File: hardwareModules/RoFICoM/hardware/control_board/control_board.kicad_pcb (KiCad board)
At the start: 4 copper layers, 193.2 x 52.8 mm, 91 parts, among them J1 SkirtConnector, J10 SENSE_A, J11 SENSE_B, J12 SENSE_1, J13 SENSE_2, J14 48V_A, J15 48V_1, J16 48V_B, J17 48V_2, J18 GND_A, J19 GND_1, J2 M+, J20 GND_B, J21 GND_2, J22 RX_A, J23 RX_B, J24 TX_1, J25 TX_2, J26 BoardSkirtConnector, J27 SkirtConnector, J28 SkirtConnector, J3 M-, J4 SYS_CONN, J5 PWR_CONN_1, J6 PWR_CONN_2, J7 SIDE_1, J8 SIDE_2, J9 SIDE_3, Q1 AP20P30Q, Q2 PNM723T703E0-2, Q3 AP20P30Q, Q4 AP20P30Q, Q5 PNM723T703E0-2, Q6 AP20P30Q, U2 DRV8837C, U3 HX6306P332MR, U6 ACS70331, U7 ACS70331, U8 VL53L1X, U9 STM32G071CBUx

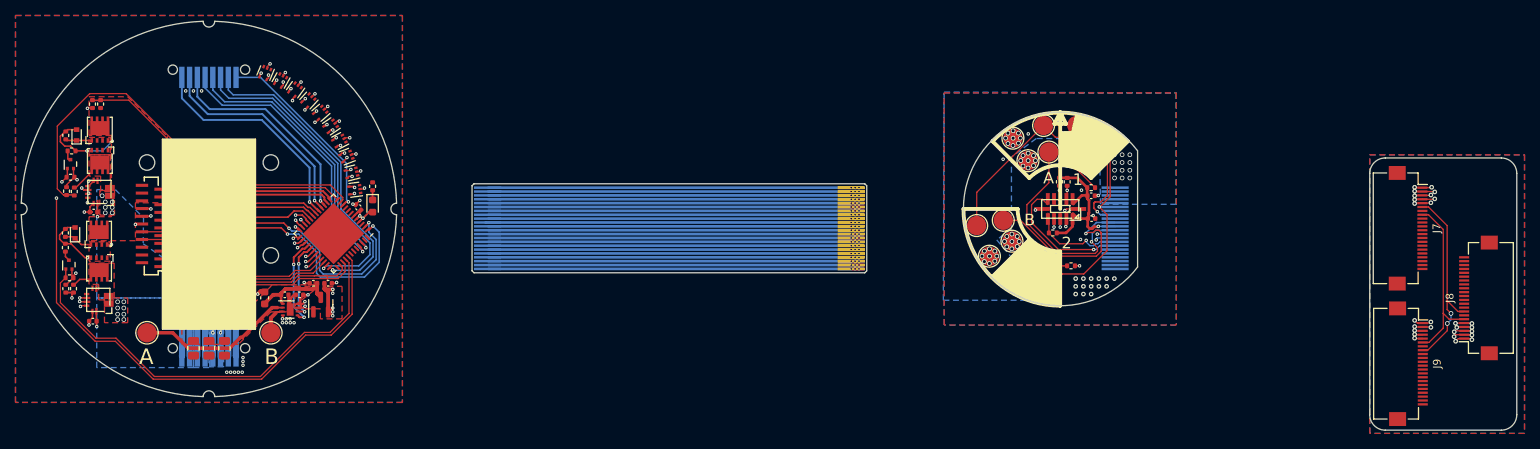
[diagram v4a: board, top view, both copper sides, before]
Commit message: roficom: Add Hall position sensor hardware
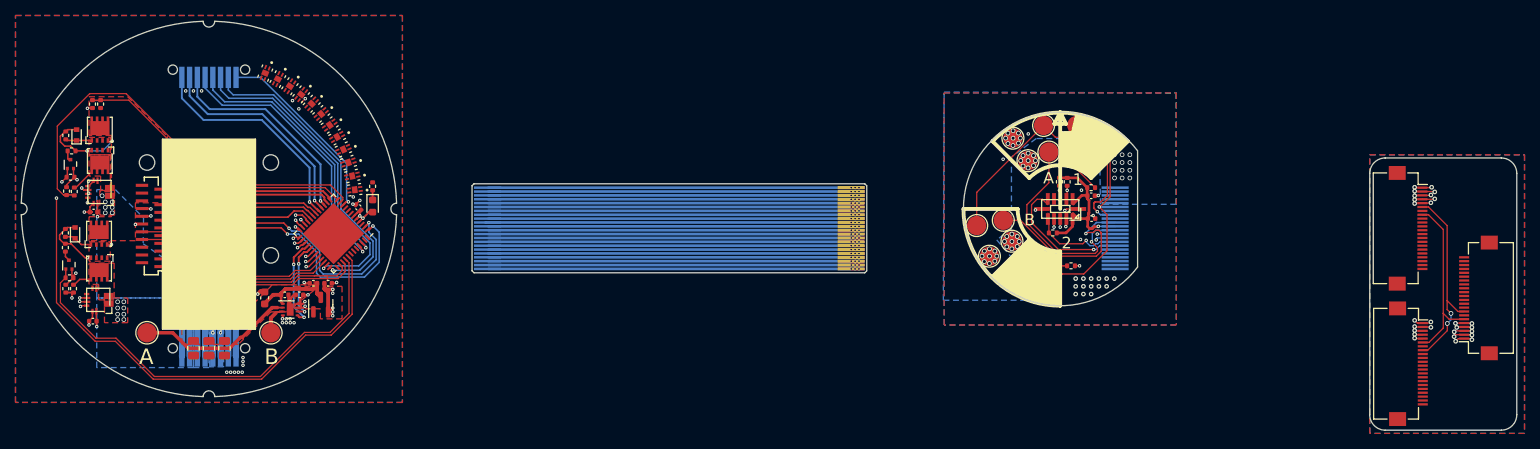
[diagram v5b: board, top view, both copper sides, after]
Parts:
- added HAL11: TMAG5231C1GQDMRR, rofi:X2SON_31H1DQDMRR_TEX, F.Cu at (98.5, 85.7)
- added HAL12: TMAG5231C1GQDMRR, rofi:X2SON_31H1DQDMRR_TEX, F.Cu at (98.8, 87.5)
- HAL1, HAL10, HAL2, HAL3, HAL4, HAL5, HAL6, HAL7, HAL8, HAL9: value KTH1611SH-SF5 -> TMAG5231C1GQDMRR; footprint Package_TO_SOT_SMD:SOT-553 -> rofi:X2SON_31H1DQDMRR_TEX
- moved HAL10 3.61 mm to (98.0, 84.0), turned to -161.591 degrees
- moved HAL9 3.21 mm to (97.4, 82.3), turned to -156.136 degrees
- moved HAL8 2.81 mm to (96.6, 80.7), turned to -150.682 degrees
- moved HAL7 2.41 mm to (95.6, 79.2), turned to -145.227 degrees
- moved HAL6 2.01 mm to (94.5, 77.7), turned to -139.773 degrees
- moved HAL5 1.61 mm to (93.3, 76.4), turned to -134.318 degrees
- moved HAL4 1.21 mm to (91.9, 75.2), turned to -128.864 degrees
- moved HAL3 0.80 mm to (90.5, 74.1), turned to -123.409 degrees
- moved HAL2 0.40 mm to (88.9, 73.2), turned to -117.955 degrees
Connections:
- HAL1 pad 1: (no net) -> GND
- HAL1 pad 2: GND -> unconnected-(HAL1-NC-Pad2)
- HAL1 pad 3: (no net) -> /position_sensor/POS1
- HAL1 pad 5: /POS1 -> unconnected-(HAL1-PAD-NC-Pad5)
- HAL10 pad 1: (no net) -> GND
- HAL10 pad 2: GND -> unconnected-(HAL10-NC-Pad2)
- HAL10 pad 3: (no net) -> /position_sensor/POS10
- HAL10 pad 5: /POS10 -> unconnected-(HAL10-PAD-NC-Pad5)
- HAL2 pad 1: (no net) -> GND
- HAL2 pad 2: GND -> unconnected-(HAL2-NC-Pad2)
- HAL2 pad 3: (no net) -> /position_sensor/POS2
- HAL2 pad 5: /POS2 -> unconnected-(HAL2-PAD-NC-Pad5)
- HAL3 pad 1: (no net) -> GND
- HAL3 pad 2: GND -> unconnected-(HAL3-NC-Pad2)
- HAL3 pad 3: (no net) -> /position_sensor/POS3
- HAL3 pad 5: /POS3 -> unconnected-(HAL3-PAD-NC-Pad5)
- HAL4 pad 1: (no net) -> GND
- HAL4 pad 2: GND -> unconnected-(HAL4-NC-Pad2)
- HAL4 pad 3: (no net) -> /position_sensor/POS4
- HAL4 pad 5: /POS4 -> unconnected-(HAL4-PAD-NC-Pad5)
- HAL5 pad 1: (no net) -> GND
- HAL5 pad 2: GND -> unconnected-(HAL5-NC-Pad2)
- HAL5 pad 3: (no net) -> /position_sensor/POS5
- HAL5 pad 5: /POS5 -> unconnected-(HAL5-PAD-NC-Pad5)
- HAL6 pad 1: (no net) -> GND
- HAL6 pad 2: GND -> unconnected-(HAL6-NC-Pad2)
- HAL6 pad 3: (no net) -> /position_sensor/POS6
- HAL6 pad 5: /POS6 -> unconnected-(HAL6-PAD-NC-Pad5)
- HAL7 pad 1: (no net) -> GND
- HAL7 pad 2: GND -> unconnected-(HAL7-NC-Pad2)
- HAL7 pad 3: (no net) -> /position_sensor/POS7
- HAL7 pad 5: /POS7 -> unconnected-(HAL7-PAD-NC-Pad5)
- HAL8 pad 1: (no net) -> GND
- HAL8 pad 2: GND -> unconnected-(HAL8-NC-Pad2)
- HAL8 pad 3: (no net) -> /position_sensor/POS8
- HAL8 pad 5: /POS8 -> unconnected-(HAL8-PAD-NC-Pad5)
- HAL9 pad 1: (no net) -> GND
- HAL9 pad 2: GND -> unconnected-(HAL9-NC-Pad2)
- HAL9 pad 3: (no net) -> /position_sensor/POS9
- HAL9 pad 5: /POS9 -> unconnected-(HAL9-PAD-NC-Pad5)
- U9 pad 21: /POS1 -> /position_sensor/POS1
- U9 pad 22: /POS2 -> /position_sensor/POS2
- U9 pad 23: /POS3 -> /position_sensor/POS3
- U9 pad 24: /POS4 -> /position_sensor/POS4
- U9 pad 25: /POS5 -> /position_sensor/POS5
- U9 pad 26: /POS6 -> /position_sensor/POS6
- U9 pad 27: /POS7 -> /position_sensor/POS7
- U9 pad 30: /POS8 -> /position_sensor/POS8
- U9 pad 31: /POS9 -> /position_sensor/POS9
- U9 pad 32: /POS10 -> /position_sensor/POS10
- U9 pad 42: unconnected-(U9-PB3-Pad42) -> /position_sensor/POS11
- U9 pad 43: unconnected-(U9-PB4-Pad43) -> /position_sensor/POS12
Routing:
- net /POS1: track 24.1 -> 0.00 mm, vias 2 -> 0
- net /position_sensor/POS1: track 0.00 -> 23.4 mm, vias 0 -> 1
- net /POS2: track 22.1 -> 0.00 mm, vias 2 -> 0
- net /POS3: track 21.6 -> 0.00 mm, vias 2 -> 0
- net /position_sensor/POS2: track 0.00 -> 21.3 mm, vias 0 -> 1
- net /position_sensor/POS3: track 0.00 -> 20.9 mm, vias 0 -> 2
- net /POS5: track 20.3 -> 0.00 mm, vias 2 -> 0
- net /POS4: track 20.2 -> 0.00 mm, vias 2 -> 0
- net /position_sensor/POS4: track 0.00 -> 20.2 mm, vias 0 -> 2
- net /position_sensor/POS5: track 0.00 -> 19.7 mm, vias 0 -> 1
- net /POS6: track 19.6 -> 0.00 mm, vias 2 -> 0
- net /position_sensor/POS6: track 0.00 -> 18.9 mm, vias 0 -> 1
- net /POS7: track 18.8 -> 0.00 mm, vias 2 -> 0
- net /position_sensor/POS7: track 0.00 -> 18.2 mm, vias 0 -> 1
- net /POS8: track 17.6 -> 0.00 mm, vias 2 -> 0
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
